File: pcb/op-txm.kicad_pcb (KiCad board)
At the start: 2 copper layers, 40 x 100 mm, 55 parts

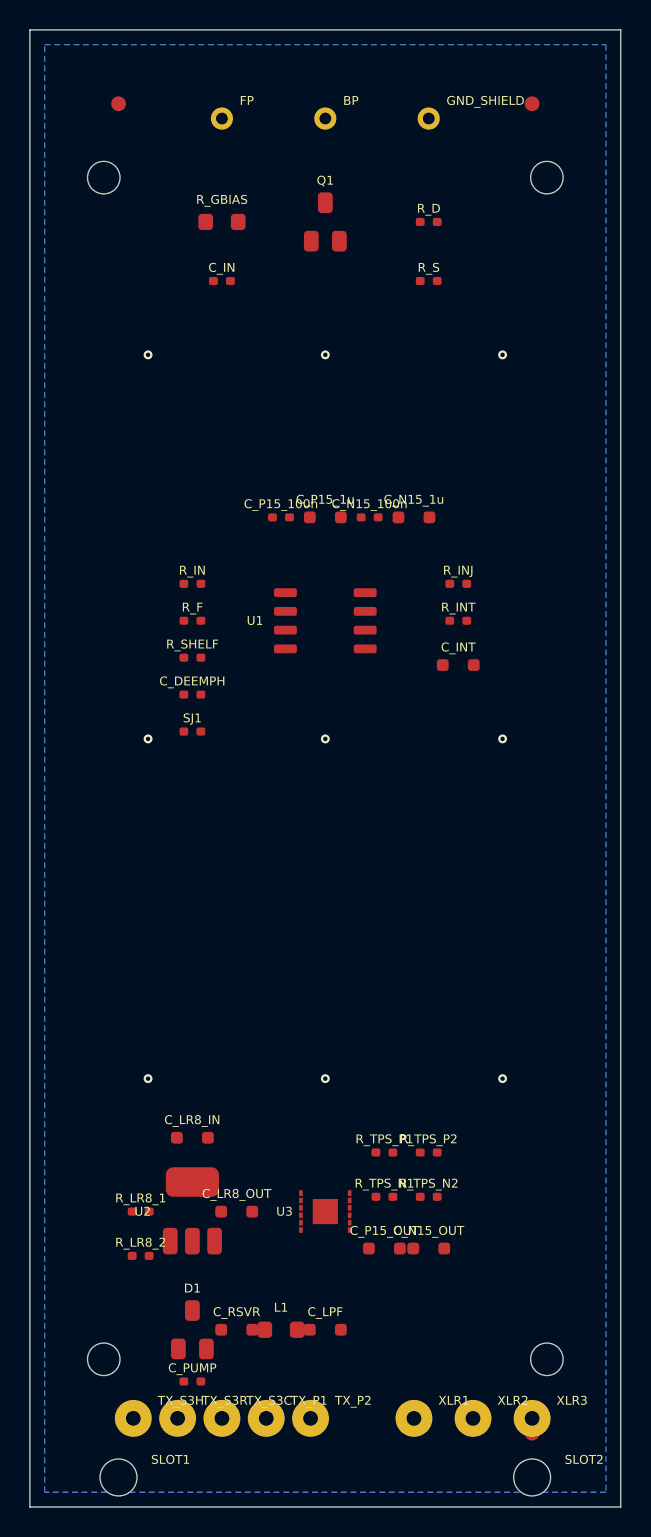
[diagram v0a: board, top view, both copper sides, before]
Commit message: Fix all courtyard overlaps; FID3 moved out of bottom-right corner
- FID3: (115,145) → (113,121) — was overlapping XLR3 and SLOT2
- Decoupling cap row Y=83: expand to 4 mm X-pitch (was 3 mm); all 0402/
  0603 courtyard gaps now 0.9 mm
- R_LR8_1/R_LR8_2: moved to (87,127)/(87,130) — were inside U2 SOT-89
  courtyard at (87.5,130)/(87.5,133)
- C_LR8_OUT: (94,130)→(96,130) — was inside U2 courtyard
- C_N15_OUT: (107,132.5)→(108,133) — was overlapping C_P15_OUT
- Charge pump row: D1@(91,138), C_RSVR@(95,138), L1@(100,138),
  C_LPF@(105,138) — 4–5 mm spacing clears all courtyard boundaries
- C_PUMP: Y=141.5→141 — clears TX_S3R/TX_S3C courtyard in Y

Result: 0 real courtyard overlaps; 4 inherent TH-pad touches at 3 mm
transformer-lead pitch (not a DRC error).

Co-Authored-By: Claude Sonnet 4.6 <noreply@anthropic.com>
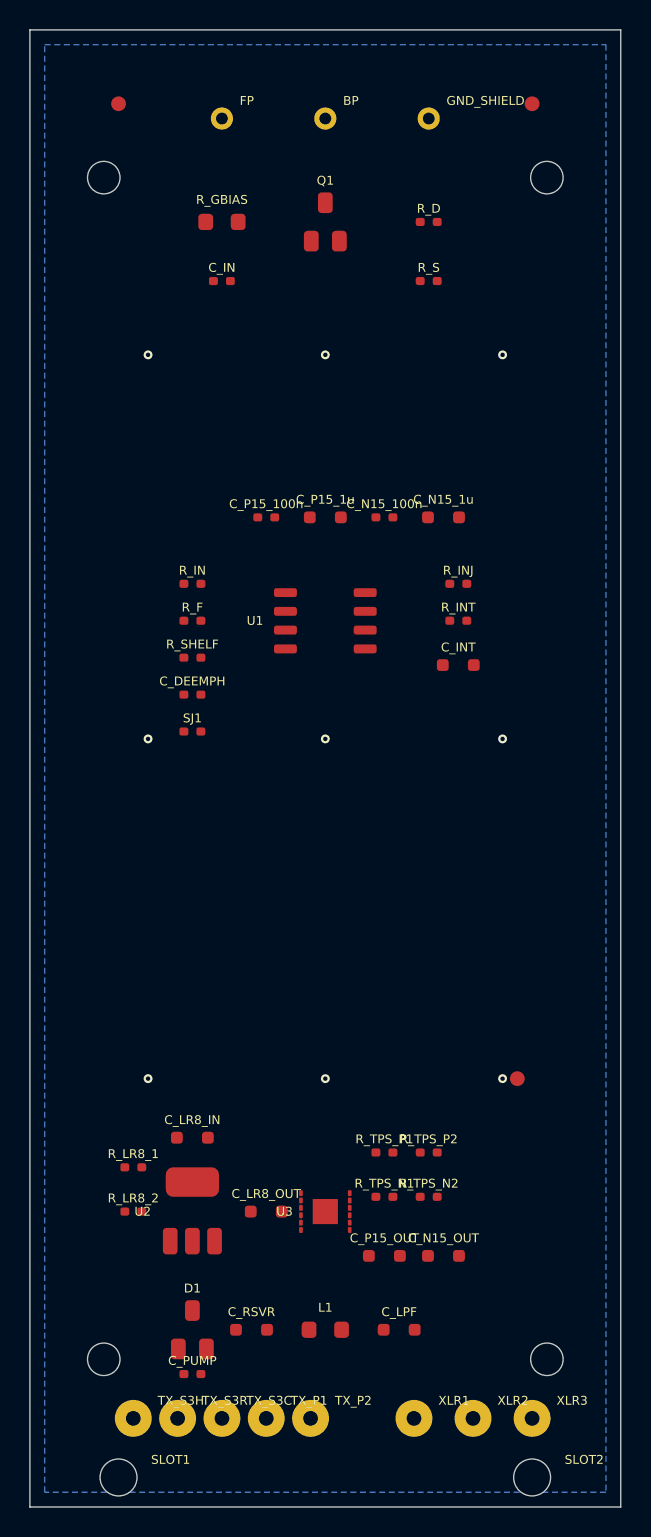
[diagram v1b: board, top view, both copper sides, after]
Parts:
- moved ? 24.0 mm to (113.0, 121.0)
- moved C_LPF 5.00 mm to (105.0, 138.0)
- moved R_LR8_1 3.04 mm to (87.0, 127.0)
- moved R_LR8_2 3.04 mm to (87.0, 130.0)
- moved L1 3.00 mm to (100.0, 138.0)
- moved C_LR8_OUT 2.00 mm to (96.0, 130.0)
- moved C_N15_1u 2.00 mm to (108.0, 83.0)
- moved C_N15_OUT 1.12 mm to (108.0, 133.0)
- moved C_N15_100n 1.00 mm to (104.0, 83.0)
- moved C_P15_100n 1.00 mm to (96.0, 83.0)
- moved C_RSVR 1.00 mm to (95.0, 138.0)
- moved C_P15_OUT 0.50 mm to (104.0, 133.0)
- moved C_PUMP 0.50 mm to (91.0, 141.0)
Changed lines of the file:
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@@
   )
   (footprint "op-txm:Fiducial" (layer "F.Cu")
-    (at 114.0 145.0)
+    (at 113.0 121.0)
     (descr "Fiducial")
     (fp_rect (start -1.5 -1.5) (end 1.5 1.5) (layer "F.CrtYd") (width 0.05))
@@
   )
   (footprint "op-txm:100n" (layer "F.Cu")
-    (at 97.0 83.0)
+    (at 96.0 83.0)
     (descr "100n")
     (fp_rect (start -1.3 -0.7) (end 1.3 0.7) (layer "F.CrtYd") (width 0.05))
@@
   )
   (footprint "op-txm:100n" (layer "F.Cu")
-    (at 103.0 83.0)
+    (at 104.0 83.0)
     (descr "100n")
     (fp_rect (start -1.3 -0.7) (end 1.3 0.7) (layer "F.CrtYd") (width 0.05))
@@
   )
   (footprint "op-txm:1u" (layer "F.Cu")
-    (at 106.0 83.0)
+    (at 108.0 83.0)
     (descr "1u")
     (fp_rect (start -1.8 -1.0) (end 1.8 1.0) (layer "F.CrtYd") (width 0.05))
@@
   )
   (footprint "op-txm:270k" (layer "F.Cu")
-    (at 87.5 130.0)
+    (at 87.0 127.0)
     (descr "270k")
     (fp_rect (start -1.3 -0.7) (end 1.3 0.7) (layer "F.CrtYd") (width 0.05))
@@
   )
   (footprint "op-txm:10k" (layer "F.Cu")
-    (at 87.5 133.0)
+    (at 87.0 130.0)
     (descr "10k")
     (fp_rect (start -1.3 -0.7) (end 1.3 0.7) (layer "F.CrtYd") (width 0.05))
@@
   )
   (footprint "op-txm:4u7" (layer "F.Cu")
-    (at 94.0 130.0)
+    (at 96.0 130.0)
     (descr "4u7")
     (fp_rect (start -1.8 -1.0) (end 1.8 1.0) (layer "F.CrtYd") (width 0.05))
@@
   )
   (footprint "op-txm:10u" (layer "F.Cu")
-    (at 104.0 132.5)
+    (at 104.0 133.0)
     (descr "10u")
     (fp_rect (start -1.8 -1.0) (end 1.8 1.0) (layer "F.CrtYd") (width 0.05))
@@
   )
   (footprint "op-txm:10u" (layer "F.Cu")
-    (at 107.0 132.5)
+    (at 108.0 133.0)
     (descr "10u")
     (fp_rect (start -1.8 -1.0) (end 1.8 1.0) (layer "F.CrtYd") (width 0.05))
@@
   )
   (footprint "op-txm:100n/100V" (layer "F.Cu")
-    (at 91.0 141.5)
+    (at 91.0 141.0)
     (descr "100n/100V")
     (fp_rect (start -1.3 -0.7) (end 1.3 0.7) (layer "F.CrtYd") (width 0.05))
@@
   )
   (footprint "op-txm:4u7/100V" (layer "F.Cu")
-    (at 94.0 138.0)
+    (at 95.0 138.0)
     (descr "4u7/100V")
     (fp_rect (start -1.8 -1.0) (end 1.8 1.0) (layer "F.CrtYd") (width 0.05))
@@
   )
   (footprint "op-txm:10mH" (layer "F.Cu")
-    (at 97.0 138.0)
+    (at 100.0 138.0)
     (descr "10mH")
     (fp_rect (start -2.2 -1.2) (end 2.2 1.2) (layer "F.CrtYd") (width 0.05))
@@
   )
   (footprint "op-txm:10u" (layer "F.Cu")
-    (at 100.0 138.0)
+    (at 105.0 138.0)
     (descr "10u")
     (fp_rect (start -1.8 -1.0) (end 1.8 1.0) (layer "F.CrtYd") (width 0.05))

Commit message: Resize PCB to 35×85 mm; reflow component placement
Board resized from 40×100 mm to 35×85 mm to fit the physical mic body,
mounting hole pattern unchanged at 30×80 mm (±15 mm X, ±40 mm Y).

All component zones compressed into the shorter board:
  - Input/JFET: Y=[60,72] (capsule pads at Y=62, same row as top MH)
  - Audio/EQ+servo: Y=[74,93] (U1 at Y=81, EQ/servo columns 2.5 mm pitch)
  - Power: Y=[100,122] (~17 mm shift up from prior layout)
  - TX area: Y=[122,135] (cutout 10×8 mm centre at Y=127, pads 3 mm pitch)

HV keepout extended to cover bottom 41 mm of the shorter board.
All 17 hole clearances verified: NPTH-to-TH-copper ≥ 2.75 mm, MH-to-TH ≥ 2.60 mm.

Co-Authored-By: Claude Sonnet 4.6 <noreply@anthropic.com>
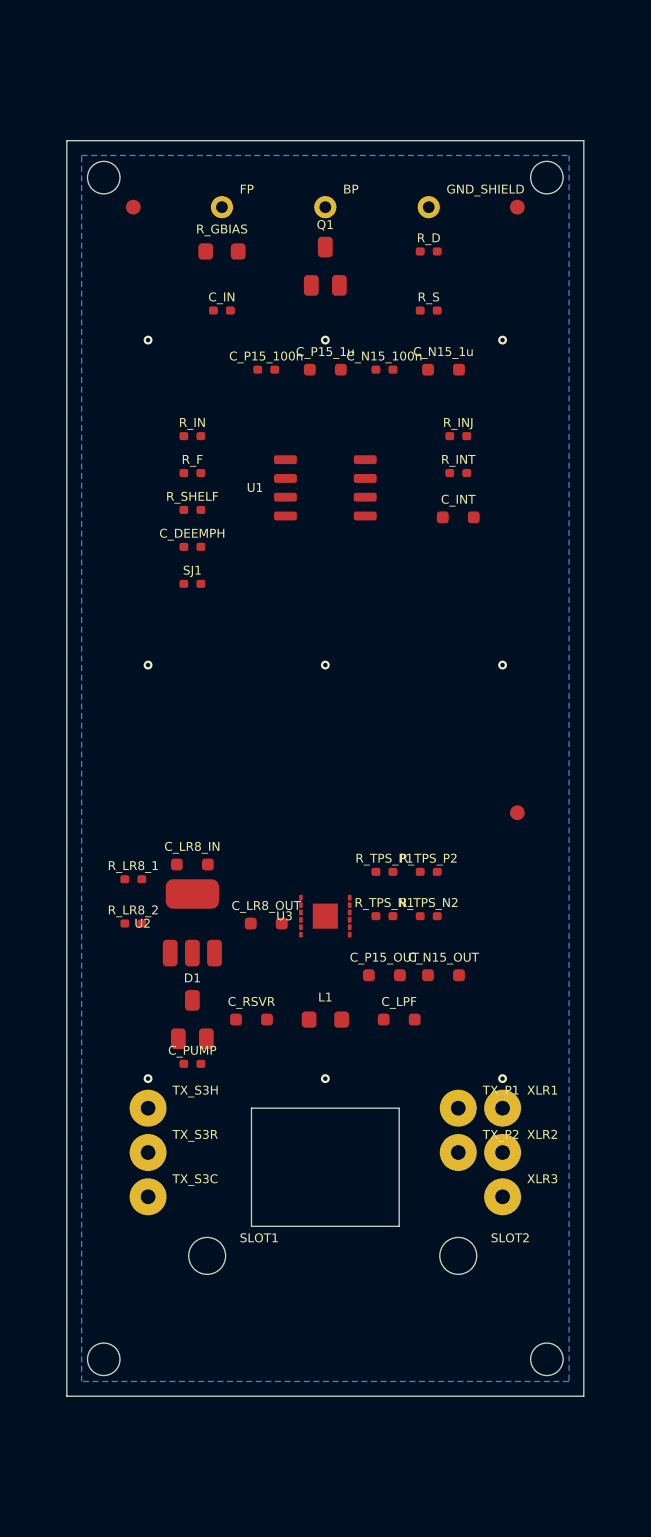
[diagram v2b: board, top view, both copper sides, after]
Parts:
- removed the ? at (86.0, 55.0)
- removed the ? at (114.0, 55.0)
- removed the ? at (113.0, 121.0)
- added ?: , op-txm:Fiducial, F.Cu at (87.0, 62.0)
- added ?: , op-txm:Fiducial, F.Cu at (113.0, 62.0)
- added ?: , op-txm:Fiducial, F.Cu at (113.0, 103.0)
- moved TX_P1 24.7 mm to (109.0, 123.0)
- moved XLR1 21.8 mm to (112.0, 123.0)
- moved TX_S3H 21.0 mm to (88.0, 123.0)
- moved C_LPF 21.0 mm to (105.0, 117.0)
- moved C_PUMP 21.0 mm to (91.0, 120.0)
- moved C_RSVR 21.0 mm to (95.0, 117.0)
- moved D1 21.0 mm to (91.0, 117.0)
- moved L1 21.0 mm to (100.0, 117.0)
- moved TX_P2 20.6 mm to (109.0, 126.0)
- moved U3 20.0 mm to (100.0, 110.0)
- moved C_LR8_OUT 19.5 mm to (96.0, 110.5)
- moved R_LR8_1 19.5 mm to (87.0, 107.5)
- moved R_LR8_2 19.5 mm to (87.0, 110.5)
- moved U2 19.5 mm to (91.0, 110.5)
- moved C_N15_OUT 19.0 mm to (108.0, 114.0)
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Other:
- board size 40 x 100 mm -> 35 x 85 mm

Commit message: Add HSMS-2820 clamp (D_RS) and route input-zone critical nets
D_RS: HSMS-2820 SOT-23 Schottky placed at (111,67) across R_S —
anode=GND, cathode=VSOURCE. Protects JFET gate-source junction during
power-up/power-down transients. Courtyard clears R_D and R_S by 1.2mm.

14 routing segments added for the JFET cluster (F.Cu):
  - VDRAIN (W_HV=0.40): Q1 drain → R_D pad1 (L-route)
  - VSOURCE (W_SIGNAL=0.20): Q1 source → R_S pad1 and D_RS cathode
    (T-node at (106.425,67.30), extends right to D_RS column at X=111)
  - VGATE (W_HIMP=0.15): R_GBIAS pad2 and C_IN pad2 → Q1 gate
    (node at Y=67.30 between the two VGATE sources)
  - GND (W_POWER=0.30): GND_SHIELD, D_RS anode, R_S pad2 → GND bus
    at X=112 terminating at GND via (112,71)

Remaining nets (BP_CAPSULE, FP_CAPSULE, audio zone, power zone)
routed interactively in KiCad.

BOM: D_RS (HSMS-2820-TR1G) added — 32 line items, 36 SMD placements.

Co-Authored-By: Claude Sonnet 4.6 <noreply@anthropic.com>
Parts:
- added D_RS: , op-txm:HSMS-2820, F.Cu at (111.0, 67.0)
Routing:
- net GND: track 0.00 -> 20.4 mm
- net VSOURCE: track 0.00 -> 13.3 mm
- net VGATE: track 0.00 -> 9.47 mm
- net VDRAIN: track 0.00 -> 6.72 mm
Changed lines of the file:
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@@
       (net 1 "GND"))
+  )
+  (footprint "op-txm:HSMS-2820" (layer "F.Cu")
+    (at 111.0 67.0)
+    (descr "HSMS-2820")
+    (fp_rect (start -1.5 -1.9) (end 1.5 2.0) (layer "F.CrtYd") (width 0.05))
+    (fp_rect (start -0.65 -0.9) (end 0.65 0.55) (layer "F.Fab") (width 0.1))
+    (fp_text reference "D_RS" (at 0 -2.8) (layer "F.SilkS")
+      (effects (font (size 0.6 0.6) (thickness 0.12)))
+    )
+    (pad "1" smd roundrect (at -0.95 1.3) (size 1.0 1.4) (layers "F.Cu" "F.Paste" "F.Mask") (roundrect_rratio 0.25)
+      (net 1 "GND"))
+    (pad "2" smd roundrect (at 0.95 1.3) (size 1.0 1.4) (layers "F.Cu" "F.Paste" "F.Mask") (roundrect_rratio 0.25)
+      (net 1 "GND"))
+    (pad "3" smd roundrect (at 0.0 -1.3) (size 1.0 1.4) (layers "F.Cu" "F.Paste" "F.Mask") (roundrect_rratio 0.25)
+      (net 7 "VSOURCE"))
   )
   (footprint "op-txm:OPA1642AIDR" (layer "F.Cu")
@@
   (gr_line (start 105 131) (end 95 131) (layer "Edge.Cuts") (width 0.05))
   (gr_line (start 95 131) (end 95 123) (layer "Edge.Cuts") (width 0.05))
+  (segment (start 100.0 64.7) (end 106.425 64.7) (width 0.4) (layer "F.Cu") (net 8))
+  (segment (start 106.425 64.7) (end 106.425 65.0) (width 0.4) (layer "F.Cu") (net 8))
+  (segment (start 100.95 67.3) (end 106.425 67.3) (width 0.2) (layer "F.Cu") (net 7))
+  (segment (start 106.425 67.3) (end 106.425 69.0) (width 0.2) (layer "F.Cu") (net 7))
+  (segment (start 106.425 67.3) (end 111.0 67.3) (width 0.2) (layer "F.Cu") (net 7))
+  (segment (start 111.0 67.3) (end 111.0 65.7) (width 0.2) (layer "F.Cu") (net 7))
+  (segment (start 94.1 65.0) (end 94.1 67.3) (width 0.15) (layer "F.Cu") (net 6))
+  (segment (start 94.1 67.3) (end 99.05 67.3) (width 0.15) (layer "F.Cu") (net 6))
+  (segment (start 93.575 69.0) (end 93.575 67.3) (width 0.15) (layer "F.Cu") (net 6))
+  (segment (start 93.575 67.3) (end 94.1 67.3) (width 0.15) (layer "F.Cu") (net 6))
+  (segment (start 112.0 62.0) (end 112.0 71.0) (width 0.3) (layer "F.Cu") (net 1))
+  (segment (start 107.0 62.0) (end 112.0 62.0) (width 0.3) (layer "F.Cu") (net 1))
+  (segment (start 110.05 68.3) (end 112.0 68.3) (width 0.3) (layer "F.Cu") (net 1))
+  (segment (start 107.575 69.0) (end 112.0 69.0) (width 0.3) (layer "F.Cu") (net 1))
   (via (at 88.0 71.0) (size 0.6) (drill 0.3) (layers "F.Cu" "B.Cu") (net 1))
   (via (at 100.0 71.0) (size 0.6) (drill 0.3) (layers "F.Cu" "B.Cu") (net 1))

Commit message: pcb: add Task A + Task F routing segments
Task A — input zone HV feeds:
- BP_CAPSULE: BP pad -> R_GBIAS pad1, detoured via X=96/Y=66.5 for 0.5 mm HV keepout from VGATE
- FP_CAPSULE: FP pad -> C_IN pad1, routed left to X=90.5 to clear BP_CAPSULE copper
- V_BOOST: R_D pad2 stub jogged to X=108.8, clears R_S GND pad by 0.5 mm

Task F — power zone PHANTOM + LR8 cluster:
- PHANTOM: C_LR8_IN pad1 <-> U2 tab <-> U2 pin3, north stub to Y=100 for Task I trunk
- P48V_LDO: U2 pin2 -> C_LR8_OUT -> R_LR8_1, routed at Y=105 above PHANTOM pads
- LR8_ADJ: R_LR8_1 pad2 -> R_LR8_2 pad1 -> U2 pin1, down-then-left to avoid pad row conflict
- GND: R_LR8_2/C_LR8_IN/C_LR8_OUT pads connected to stitching vias; local via at (93.6,108.5)

Co-Authored-By: Claude Sonnet 4.6 <noreply@anthropic.com>
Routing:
- net GND: track 20.4 -> 48.4 mm, vias 9 -> 10
- net P48V_LDO: track 0.00 -> 22.5 mm
- net PHANTOM: track 0.00 -> 15.0 mm
- net BP_CAPSULE: track 0.00 -> 14.1 mm
- net FP_CAPSULE: track 0.00 -> 11.4 mm
- net LR8_ADJ: track 0.00 -> 9.23 mm
- net V_BOOST: track 0.00 -> 7.22 mm
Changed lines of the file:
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@@
   (segment (start 110.05 68.3) (end 112.0 68.3) (width 0.3) (layer "F.Cu") (net 1))
   (segment (start 107.575 69.0) (end 112.0 69.0) (width 0.3) (layer "F.Cu") (net 1))
+  (segment (start 100.0 62.0) (end 96.0 62.0) (width 0.4) (layer "F.Cu") (net 20))
+  (segment (start 96.0 62.0) (end 96.0 66.5) (width 0.4) (layer "F.Cu") (net 20))
+  (segment (start 96.0 66.5) (end 91.9 66.5) (width 0.4) (layer "F.Cu") (net 20))
+  (segment (start 91.9 66.5) (end 91.9 65.0) (width 0.4) (layer "F.Cu") (net 20))
+  (segment (start 93.0 62.0) (end 93.0 63.5) (width 0.15) (layer "F.Cu") (net 21))
+  (segment (start 93.0 63.5) (end 90.5 63.5) (width 0.15) (layer "F.Cu") (net 21))
+  (segment (start 90.5 63.5) (end 90.5 69.0) (width 0.15) (layer "F.Cu") (net 21))
+  (segment (start 90.5 69.0) (end 92.425 69.0) (width 0.15) (layer "F.Cu") (net 21))
+  (segment (start 107.575 65.0) (end 108.8 65.0) (width 0.4) (layer "F.Cu") (net 3))
+  (segment (start 108.8 65.0) (end 108.8 71.0) (width 0.4) (layer "F.Cu") (net 3))
+  (segment (start 89.95 106.5) (end 89.95 100.0) (width 0.4) (layer "F.Cu") (net 2))
+  (segment (start 89.95 106.5) (end 89.95 108.5) (width 0.4) (layer "F.Cu") (net 2))
+  (segment (start 89.95 108.5) (end 91.0 108.5) (width 0.4) (layer "F.Cu") (net 2))
+  (segment (start 91.0 108.5) (end 92.5 108.5) (width 0.4) (layer "F.Cu") (net 2))
+  (segment (start 92.5 108.5) (end 92.5 112.5) (width 0.4) (layer "F.Cu") (net 2))
+  (segment (start 91.0 112.5) (end 91.0 110.5) (width 0.3) (layer "F.Cu") (net 12))
+  (segment (start 91.0 110.5) (end 94.95 110.5) (width 0.3) (layer "F.Cu") (net 12))
+  (segment (start 94.95 110.5) (end 94.95 105.0) (width 0.3) (layer "F.Cu") (net 12))
+  (segment (start 94.95 105.0) (end 86.425 105.0) (width 0.3) (layer "F.Cu") (net 12))
+  (segment (start 86.425 105.0) (end 86.425 107.5) (width 0.3) (layer "F.Cu") (net 12))
+  (segment (start 87.575 107.5) (end 87.575 109.0) (width 0.2) (layer "F.Cu") (net 13))
+  (segment (start 87.575 109.0) (end 86.425 109.0) (width 0.2) (layer "F.Cu") (net 13))
+  (segment (start 86.425 109.0) (end 86.425 112.5) (width 0.2) (layer "F.Cu") (net 13))
+  (segment (start 86.425 112.5) (end 89.5 112.5) (width 0.2) (layer "F.Cu") (net 13))
+  (segment (start 87.575 110.5) (end 88.0 110.5) (width 0.3) (layer "F.Cu") (net 1))
+  (segment (start 88.0 110.5) (end 88.0 121.0) (width 0.3) (layer "F.Cu") (net 1))
+  (segment (start 92.05 106.5) (end 93.6 106.5) (width 0.3) (layer "F.Cu") (net 1))
+  (segment (start 93.6 106.5) (end 93.6 108.5) (width 0.3) (layer "F.Cu") (net 1))
+  (segment (start 97.05 110.5) (end 97.0 110.5) (width 0.3) (layer "F.Cu") (net 1))
+  (segment (start 97.0 110.5) (end 97.0 121.0) (width 0.3) (layer "F.Cu") (net 1))
+  (segment (start 97.0 121.0) (end 100.0 121.0) (width 0.3) (layer "F.Cu") (net 1))
   (via (at 88.0 71.0) (size 0.6) (drill 0.3) (layers "F.Cu" "B.Cu") (net 1))
   (via (at 100.0 71.0) (size 0.6) (drill 0.3) (layers "F.Cu" "B.Cu") (net 1))
@@
   (via (at 100.0 121.0) (size 0.6) (drill 0.3) (layers "F.Cu" "B.Cu") (net 1))
   (via (at 112.0 121.0) (size 0.6) (drill 0.3) (layers "F.Cu" "B.Cu") (net 1))
+  (via (at 93.6 108.5) (size 0.6) (drill 0.3) (layers "F.Cu" "B.Cu") (net 1))
   (zone (net 0) (net_name "HV_Keepout") (layer "F.Cu") (name "HV_Keepout") (hatch edge 0.508)
     (connect_pads (clearance 0.25))
